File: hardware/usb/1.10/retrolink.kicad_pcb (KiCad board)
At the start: 2 copper layers, 43 x 28 mm, 5 parts, among them J1 DE9_Socket, J2 USB_A

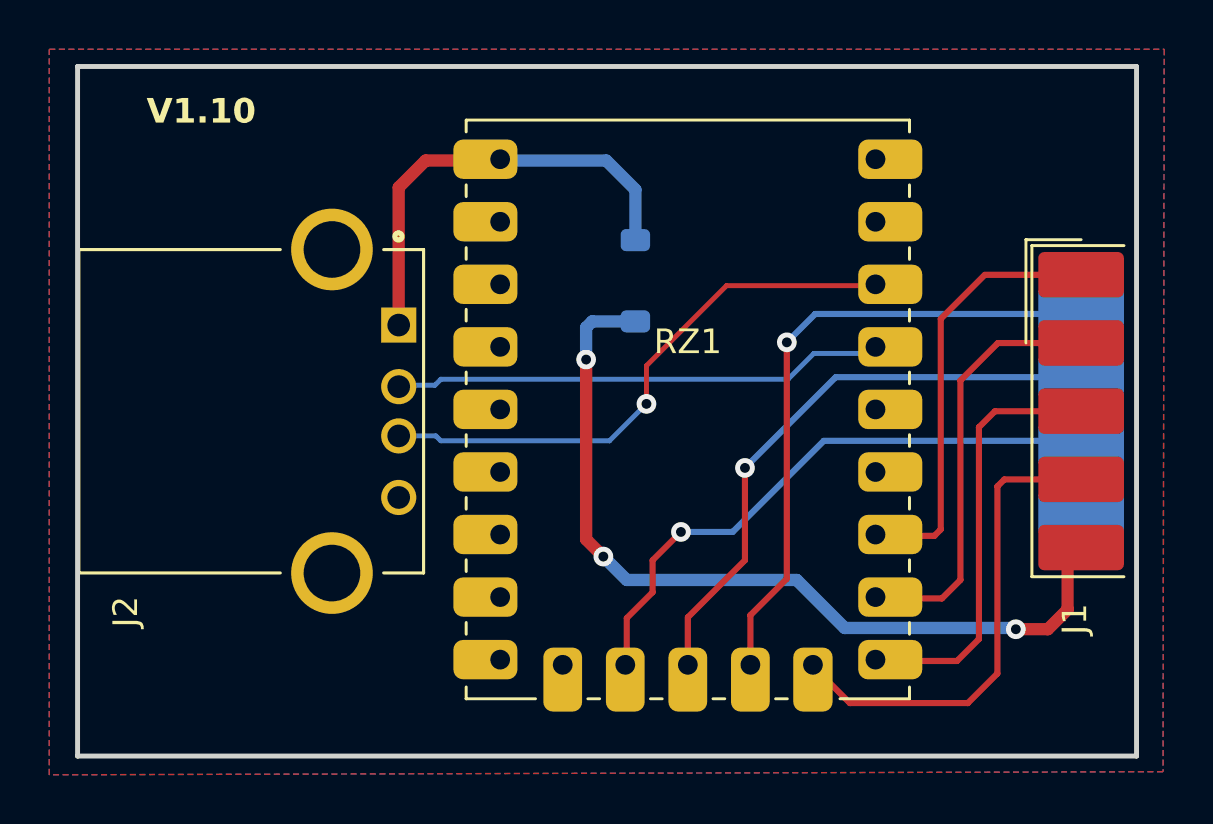
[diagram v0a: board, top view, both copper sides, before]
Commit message: - Reassigned USB-A host D+/D- from GPIO2/GPIO3 to GPIO27/GPIO28; the current build requires matching updated wiring instead of the original hardware revision `1.00` data pair. - Remapped MSX up/A/down/B/left/OUT/right to GPIO0/1/2/3/4/5/6 and removed unused GPIO4/5 VBUS reservations; updated wiring is required and OUT remains unused in joystick mode.
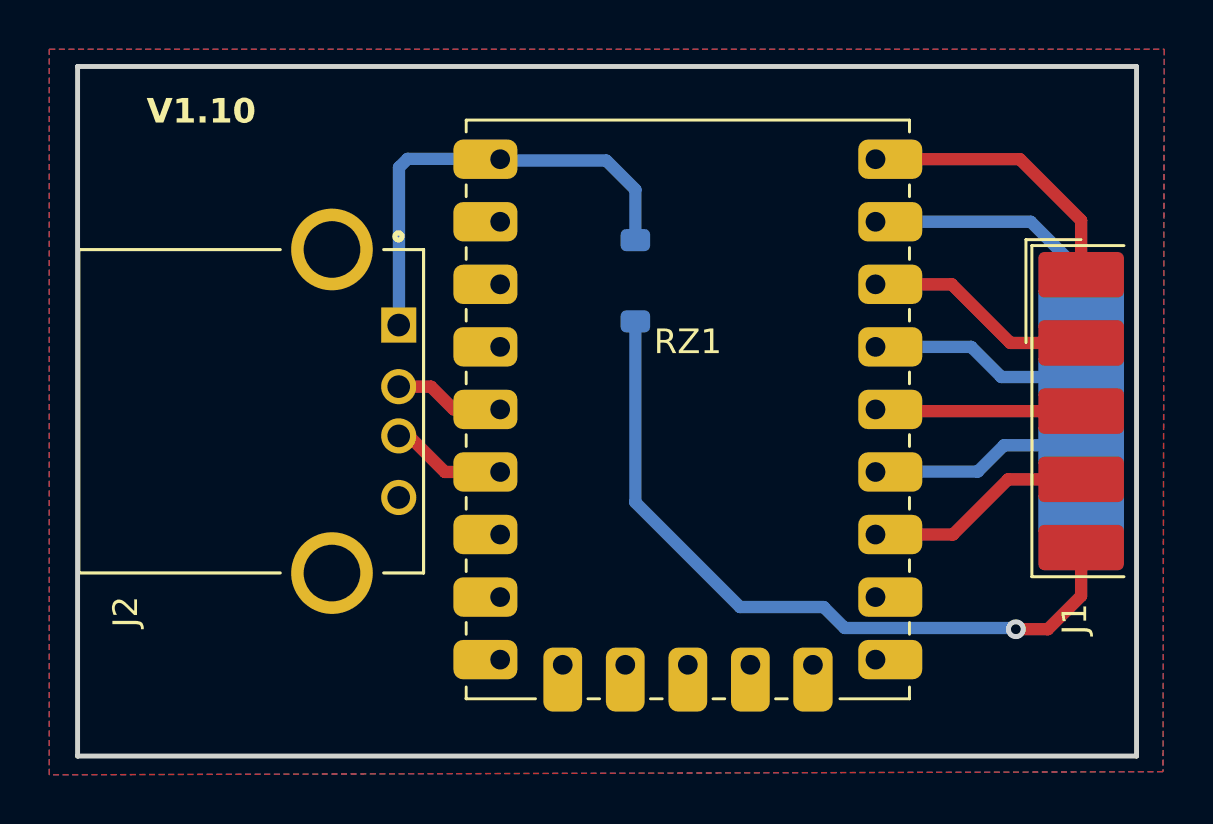
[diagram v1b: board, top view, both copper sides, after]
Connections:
- RZ1 pad 1: unconnected-(RZ1-GP0-Pad1) -> /MSX_UP
- RZ1 pad 10: /MSX_RIGHT -> unconnected-(RZ1-GP9-Pad10)
- RZ1 pad 11: /MSX_A -> unconnected-(RZ1-GP10-Pad11)
- RZ1 pad 12: /MSX_B -> unconnected-(RZ1-GP11-Pad12)
- RZ1 pad 13: /MSX_OUT -> unconnected-(RZ1-GP12-Pad13)
- RZ1 pad 18: unconnected-(RZ1-GP27-Pad18) -> /USBD+
- RZ1 pad 19: unconnected-(RZ1-GP28-Pad19) -> /USBD-
- RZ1 pad 2: unconnected-(RZ1-GP1-Pad2) -> /MSX_A
- RZ1 pad 3: /USBD+ -> /MSX_DOWN
- RZ1 pad 4: /USBD- -> /MSX_B
- RZ1 pad 5: unconnected-(RZ1-GP4-Pad5) -> /MSX_LEFT
- RZ1 pad 6: unconnected-(RZ1-GP5-Pad6) -> /MSX_OUT
- RZ1 pad 7: /MSX_UP -> /MSX_RIGHT
- RZ1 pad 8: /MSX_DOWN -> unconnected-(RZ1-GP7-Pad8)
- RZ1 pad 9: /MSX_LEFT -> unconnected-(RZ1-GP8-Pad9)
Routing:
- net /USBD+: track 23.0 -> 4.78 mm, vias 1 -> 0
- net /USBD-: track 20.0 -> 4.50 mm
- net /MSX_A: track 25.7 -> 11.0 mm, vias 1 -> 0
- net /MSX_OUT: track 23.7 -> 9.06 mm, vias 1 -> 0
- net /MSX_B: track 23.6 -> 9.15 mm, vias 1 -> 0
- net /MSX_RIGHT: track 19.2 -> 9.28 mm
- net /MSX_LEFT: track 17.0 -> 8.38 mm
- net /MSX_DOWN: track 16.8 -> 9.34 mm
- net /MSX_UP: track 17.2 -> 11.6 mm
- net Net-(D1-A): track 34.6 -> 30.7 mm, vias 3 -> 1
- net +5V: track 18.1 -> 18.7 mm

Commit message: Add RetroLink MD firmware and testing framework
- Introduced CMakeLists.txt for building the RetroLink MD project with support for regression tests.
- Created a Makefile for building the project on different platforms.
- Added board configuration header defining GPIO mappings and hardware revision.
- Implemented MD pad handling with md_pad.h and md_pad.c for decoding button states.
- Developed md_port.h and md_port.c for interfacing with the MD port and reading input.
- Created msx_output.h and msx_output.c for managing MSX joystick output.
- Implemented main.c to initialize components and handle polling logic.
- Added unit tests for md_pad functionality in md_pad_test.c.
- Developed integration tests for md_io in md_io_test.c to validate GPIO interactions.
- Included stub implementations for GPIO and timing functions to facilitate testing.
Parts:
- added kibuzzard-6AB40DA5: G***, kibuzzard-6AB40DA5, F.Cu at (109.8, 99.3)
